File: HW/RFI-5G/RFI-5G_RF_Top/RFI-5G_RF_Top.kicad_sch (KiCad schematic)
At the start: 32 parts, among them J1 Conn_01x03, J2 Conn_01x02, J3 Conn_01x06_Female, J4 Conn_01x03, J5 SMP, J6 Conn_01x10, U1 HMC342, U2 HMC342, U3 HMC260, U4 CY2-44+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

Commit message: PL boards
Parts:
- removed J1, J4: Conn_01x03, Connector_PinHeader_2.54mm:PinHeader_1x03_P2.54mm_Vertical, symbol Connector_Generic:Conn_01x03
- removed J2: Conn_01x02, Connector_PinHeader_2.54mm:PinHeader_1x02_P2.54mm_Vertical, symbol Connector_Generic:Conn_01x02
- removed J3: Conn_01x06_Female, Connector_PinHeader_1.00mm:PinHeader_1x06_P1.00mm_Vertical, symbol Connector:Conn_01x06_Female
- removed J6: Conn_01x10, Connector_PinHeader_2.54mm:PinHeader_1x10_P2.54mm_Vertical, symbol Connector_Generic:Conn_01x10
- added J1: Conn_01x09_Female, Connector_PinSocket_1.00mm:PinSocket_1x09_P1.00mm_Vertical, symbol Connector:Conn_01x09_Female
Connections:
- net 3V: now also J1.7 (Pin_7)
- net GND: now also J1.6 (Pin_6)
- net SCL: now also J1.9 (Pin_9)
- net SDA: now also J1.8 (Pin_8)
- net VTune1: now also J1.1 (Pin_1)
- net Vcc_LNA1: now also C1.1, C2.1, C3.1, U1.21 (Vdd), J1.5 (Pin_5)
- net Vcc_LNA2: now also C4.1, C5.1, C6.1, U2.21 (Vdd), J1.4 (Pin_4)
- net Vcc_LO1Amp: now also J1.3 (Pin_3)
- net Vcc_VCO: now also J1.2 (Pin_2)
- removed net Vcc_LNA: C1.1, C2.1, C3.1, C4.1, C5.1, C6.1, U1.21 (Vdd), U2.21 (Vdd)
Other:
- note added: "RF Connectors"
- note removed: "PoquetQube Connectors"
- note removed: "RF Connector"
- moved on the sheet: C15, J5, U6

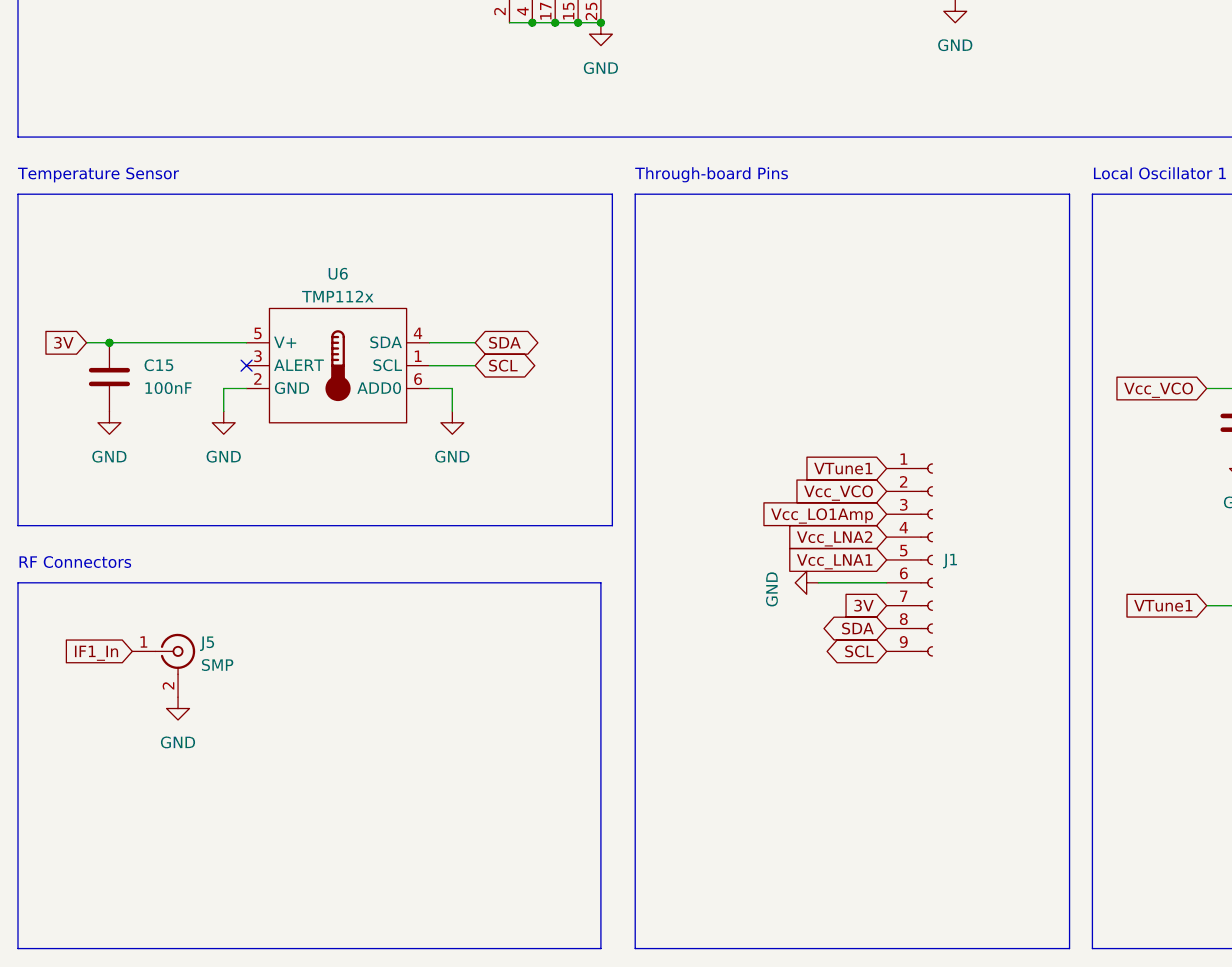
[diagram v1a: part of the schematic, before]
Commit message: All boards dseigned, thickness change pending
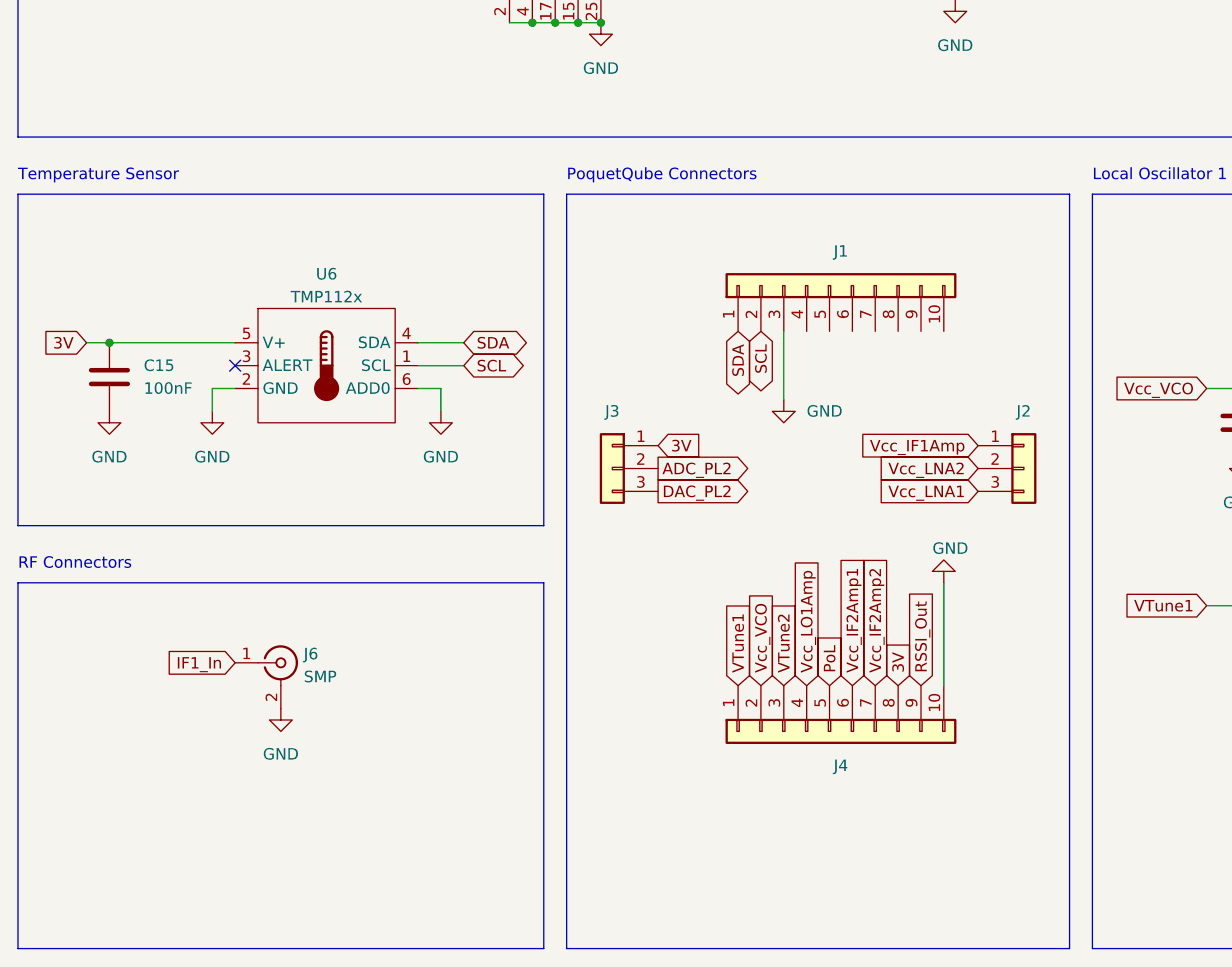
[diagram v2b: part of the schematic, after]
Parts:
- removed J1: Conn_01x09_Female, Connector_PinSocket_1.00mm:PinSocket_1x09_P1.00mm_Vertical, symbol Connector:Conn_01x09_Female
- added J1, J4: Conn_01x10, Connector_PinHeader_2.54mm:PinHeader_1x10_P2.54mm_Vertical, symbol Connector_Generic:Conn_01x10
- added J2, J3: Conn_01x03, Connector_PinHeader_2.54mm:PinHeader_1x03_P2.54mm_Vertical, symbol Connector_Generic:Conn_01x03
- renumbered J5 to J6
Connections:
- net 3V: now also J3.1 (Pin_1), J4.8 (Pin_8)
- net GND: now also J1.3 (Pin_3), J4.10 (Pin_10)
- net SCL: now also J1.2 (Pin_2)
- net SDA: now also J1.1 (Pin_1)
- net VTune1: now also J4.1 (Pin_1)
- net Vcc_LNA1: now also J2.3 (Pin_3)
- net Vcc_LNA2: now also J2.2 (Pin_2)
- net Vcc_LO1Amp: now also J4.4 (Pin_4)
- net Vcc_VCO: now also J4.2 (Pin_2)
- new net ADC_PL2: J3.2 (Pin_2)
- new net DAC_PL2: J3.3 (Pin_3)
- new net PoL: J4.5 (Pin_5)
- new net RSSI_Out: J4.9 (Pin_9)
- new net VTune2: J4.3 (Pin_3)
- new net Vcc_IF1Amp: J2.1 (Pin_1)
- new net Vcc_IF2Amp1: J4.6 (Pin_6)
- new net Vcc_IF2Amp2: J4.7 (Pin_7)
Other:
- note added: "PoquetQube Connectors"
- note removed: "Through-board Pins"
- moved on the sheet: J6, U6

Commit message: almost finished PCB's
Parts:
- added H1, H2, H3, H4: MountingHole_Pad, symbol Mechanical:MountingHole_Pad
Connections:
- net GND: now also H1.1, H2.1, H3.1, H4.1
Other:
- note added: "Mounting Holes"
- moved on the sheet: J6
